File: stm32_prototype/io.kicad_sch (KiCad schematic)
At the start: 14 parts, among them J1 USB-C, U2 USBLC6-2SC6, U3 AP2112K-3.3

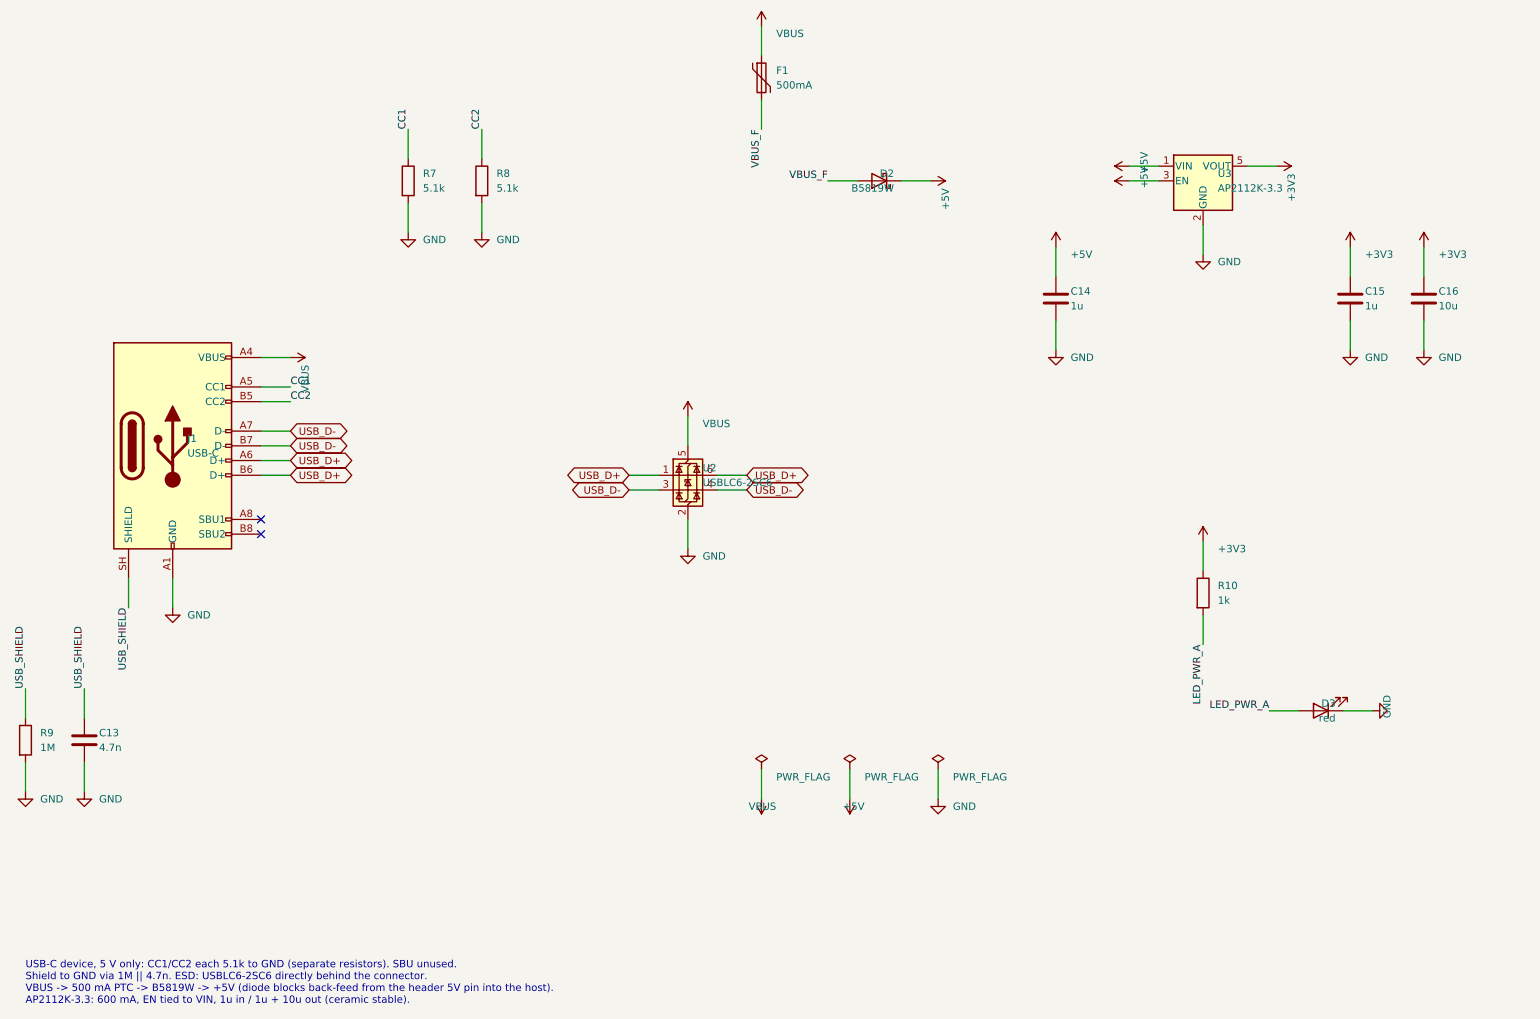
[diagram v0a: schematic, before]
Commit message: Rev C schematic: STM32 RC-car controller
- New sheets power / drive / io replace power_usb / connectors
- 2S-3S battery on XT30 with AO4407A reverse protection, SMAJ15A, VBAT sense divider
- TPS563201 5 V / 3 A buck for servos and receiver; logic 5 V ORed from servo rail and USB
- DRV8870 brushed motor driver (3.3 A trip), 4 servo/ESC outputs, 3 receiver inputs,
  2 low-side light outputs, LSM6DS3TR-C IMU on I2C2, UART and 2x5 expansion header
- Project symbol library rcboard.kicad_sym (DRV8870, AO4407A)
- ERC 0/0, netlist matches all 74 intended nets (scripts/revc_schematic)

Co-Authored-By: Claude Opus 5.5 (1M context) <noreply@anthropic.com>
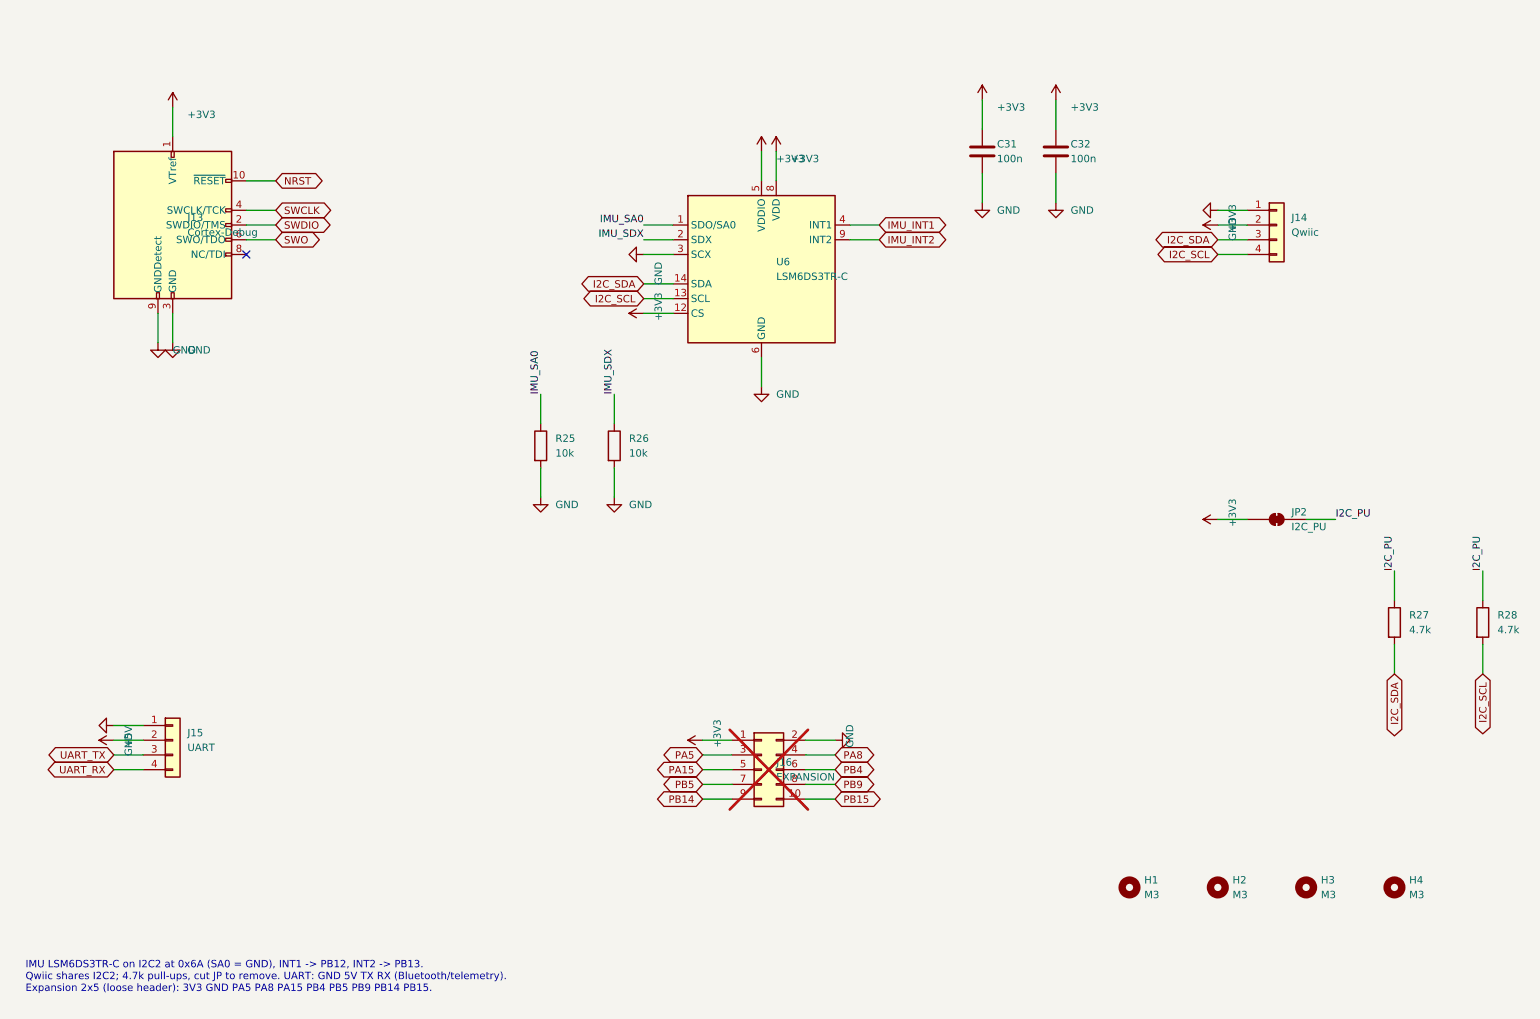
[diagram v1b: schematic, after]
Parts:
- removed C13: 4.7n, Capacitor_SMD:C_0603_1608Metric, symbol Device:C
- removed C14, C15: 1u, Capacitor_SMD:C_0603_1608Metric, symbol Device:C
- removed C16: 10u, Capacitor_SMD:C_0603_1608Metric, symbol Device:C
- removed D2: B5819W, Diode_SMD:D_SOD-123, symbol Device:D_Schottky
- removed D3: red, LED_SMD:LED_0603_1608Metric, symbol Device:LED
- removed F1: 500mA, Fuse:Fuse_1206_3216Metric, symbol Device:Polyfuse
- removed J1: USB-C, Connector_USB:USB_C_Receptacle_HRO_TYPE-C-31-M-12, symbol Connector:USB_C_Receptacle_USB2.0_16P
- removed R10: 1k, Resistor_SMD:R_0603_1608Metric, symbol Device:R
- removed R7, R8: 5.1k, Resistor_SMD:R_0603_1608Metric, symbol Device:R
- removed R9: 1M, Resistor_SMD:R_0603_1608Metric, symbol Device:R
- removed U2: USBLC6-2SC6, Package_TO_SOT_SMD:SOT-23-6, symbol Power_Protection:USBLC6-2SC6
- removed U3: AP2112K-3.3, Package_TO_SOT_SMD:SOT-23-5, symbol Regulator_Linear:AP2112K-3.3
- added C31, C32: 100n, Capacitor_SMD:C_0603_1608Metric, symbol Device:C
- added H1, H2, H3, H4: M3, MountingHole:MountingHole_3.2mm_M3, symbol Mechanical:MountingHole
- added J13: Cortex-Debug, Connector_PinHeader_1.27mm:PinHeader_2x05_P1.27mm_Vertical_SMD, symbol Connector:Conn_ARM_JTAG_SWD_10
- added J14: Qwiic, Connector_JST:JST_SH_SM04B-SRSS-TB_1x04-1MP_P1.00mm_Horizontal, symbol Connector_Generic:Conn_01x04
- added J15: UART, Connector_PinHeader_2.54mm:PinHeader_1x04_P2.54mm_Vertical, symbol Connector_Generic:Conn_01x04
- added J16: EXPANSION, Connector_PinHeader_2.54mm:PinHeader_2x05_P2.54mm_Vertical, symbol Connector_Generic:Conn_02x05_Odd_Even
- added JP2: I2C_PU, Jumper:SolderJumper-2_P1.3mm_Bridged_RoundedPad1.0x1.5mm, symbol Jumper:SolderJumper_2_Bridged
- added R25, R26: 10k, Resistor_SMD:R_0603_1608Metric, symbol Device:R
- added R27, R28: 4.7k, Resistor_SMD:R_0603_1608Metric, symbol Device:R
- added U6: LSM6DS3TR-C, Package_LGA:LGA-14_3x2.5mm_P0.5mm_LayoutBorder3x4y, symbol Sensor_Motion:LSM6DS3
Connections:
- net +3V3: now also C31.1, C32.1, J13.1 (VTref), J14.2 (Pin_2), J16.1 (Pin_1), JP2.1 (A), U6.12 (CS), U6.5 (VDDIO), U6.8 (VDD)
- net +5V: now also J15.2 (Pin_2)
- net GND: now also C31.2, C32.2, J13.3 (GND), J13.5 (GND), J13.9 (GNDDetect), J14.1 (Pin_1), J15.1 (Pin_1), J16.2 (Pin_2), R25.2, R26.2, U6.3 (SCX), U6.6 (GND), U6.7 (GND)
- new net I2C_PU: JP2.2 (B), R27.1, R28.1
- new net I2C_SCL: J14.4 (Pin_4), R28.2, U6.13 (SCL)
- new net I2C_SDA: J14.3 (Pin_3), R27.2, U6.14 (SDA)
- new net IMU_INT1: U6.4 (INT1)
- new net IMU_INT2: U6.9 (INT2)
- new net IMU_SA0: R25.1, U6.1 (SDO/SA0)
- new net IMU_SDX: R26.1, U6.2 (SDX)
- new net NRST: J13.10 (~{RESET})
- new net PA15: J16.5 (Pin_5)
- new net PA5: J16.3 (Pin_3)
- new net PA8: J16.4 (Pin_4)
- new net PB14: J16.9 (Pin_9)
- new net PB15: J16.10 (Pin_10)
- new net PB4: J16.6 (Pin_6)
- new net PB5: J16.7 (Pin_7)
- new net PB9: J16.8 (Pin_8)
- new net SWCLK: J13.4 (SWCLK/TCK)
- new net SWDIO: J13.2 (SWDIO/TMS)
- new net SWO: J13.6 (SWO/TDO)
- new net UART_RX: J15.4 (Pin_4)
- new net UART_TX: J15.3 (Pin_3)
- no-connect marks 2 -> 1
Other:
- note added: "IMU LSM6DS3TR-C on I2C2 at 0x6A (SA0 = GND), INT1 -> PB12, INT2 -> PB13. Qwiic shares I2C2; 4.7k pull-ups, cut JP to remove. UART: GND 5V TX RX (Bluetooth/telemetry). Expansion 2x5 (loose header): 3V3 GND PA5 PA8 PA15 PB4 PB5 PB9 PB14 PB15."
- note removed: "USB-C device, 5 V only: CC1/CC2 each 5.1k to GND (separate resistors). SBU unused. Shield to GND via 1M || 4.7n. ESD: USBLC6-2SC6 directly behind the connector. VBUS -> 500 mA PTC -> B5819W -> +5V (diode blocks back-feed from the header 5V pin into the host). AP2112K-3.3: 600 mA, EN tied to VIN, 1u in / 1u + 10u out (ceramic stable)."
- title: USB-C and power supply -> Debug, IMU, Qwiic, UART, expansion

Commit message: Rev C: WS2812 RGB lighting output for 6 LEDs
- PA8 (TIM1 CH1 + DMA) -> SN74AHCT1G125 at 5 V -> 330R -> 3-pin connector (5V, DIN, GND),
  22 uF at the connector; PA8 removed from the expansion header
- Board re-placed and re-routed: DRC 0 violations, 0 unconnected, 0 parity issues; bottom silk 'RGB 5V DI G'
- Firmware: 800 kHz WS2812 driver via DMA, default head/sill/tail colours, 'c' colour and 'ind' indicator
  commands; builds (30 KB flash)
- Fabrication data, schematic images, renders and docs updated

Co-Authored-By: Claude Opus 5.5 (1M context) <noreply@anthropic.com>
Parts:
- added C33: 100n, Capacitor_SMD:C_0603_1608Metric, symbol Device:C
- added C34: 22u 25V, Capacitor_SMD:C_1206_3216Metric, symbol Device:C
- added H2: M3, MountingHole:MountingHole_3.2mm_M3, symbol Mechanical:MountingHole
- added J17: WS2812, Connector_PinHeader_2.54mm:PinHeader_1x03_P2.54mm_Vertical, symbol Connector_Generic:Conn_01x03
- added R29: 330R, Resistor_SMD:R_0603_1608Metric, symbol Device:R
- U7: renamed from H2; value M3 -> SN74AHCT1G125; footprint MountingHole:MountingHole_3.2mm_M3 -> Package_TO_SOT_SMD:SOT-23-5; symbol Mechanical:MountingHole -> 74xGxx:74AHCT1G125; LCSC (none) -> C7484; MPN (none) -> SN74AHCT1G125DBVR; now in the parts list
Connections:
- net PA8 is gone; now on net GND: J16.4 (Pin_4)
- net +5V: now also U7.5 (VCC), C33.1
- net GND: now also U7.1, U7.3 (GND), C33.2, C34.2, J17.3 (Pin_3)
- new net LED_BUF: R29.1, U7.4
- new net LED_DATA: U7.2
- new net LED_DIN: J17.2 (Pin_2), R29.2
- new net V5_SERVO: C34.1, J17.1 (Pin_1)
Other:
- note added: "IMU LSM6DS3TR-C on I2C2 at 0x6A (SA0 = GND), INT1 -> PB12, INT2 -> PB13. Qwiic shares I2C2; 4.7k pull-ups, cut JP to remove. UART: GND 5V TX RX (Bluetooth/telemetry). Expansion 2x5 (loose header): 3V3 GND PA5 GND PA15 PB4 PB5 PB9 PB14 PB15. WS2812 output: 5V, DIN, GND. PA8 (TIM1 CH1, DMA) -> 74AHCT1G125 (5 V levels) -> 330R. 6 LEDs ~0.36 A."
- note removed: "IMU LSM6DS3TR-C on I2C2 at 0x6A (SA0 = GND), INT1 -> PB12, INT2 -> PB13. Qwiic shares I2C2; 4.7k pull-ups, cut JP to remove. UART: GND 5V TX RX (Bluetooth/telemetry). Expansion 2x5 (loose header): 3V3 GND PA5 PA8 PA15 PB4 PB5 PB9 PB14 PB15."
